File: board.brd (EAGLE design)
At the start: 50 x 50 mm, 8 parts

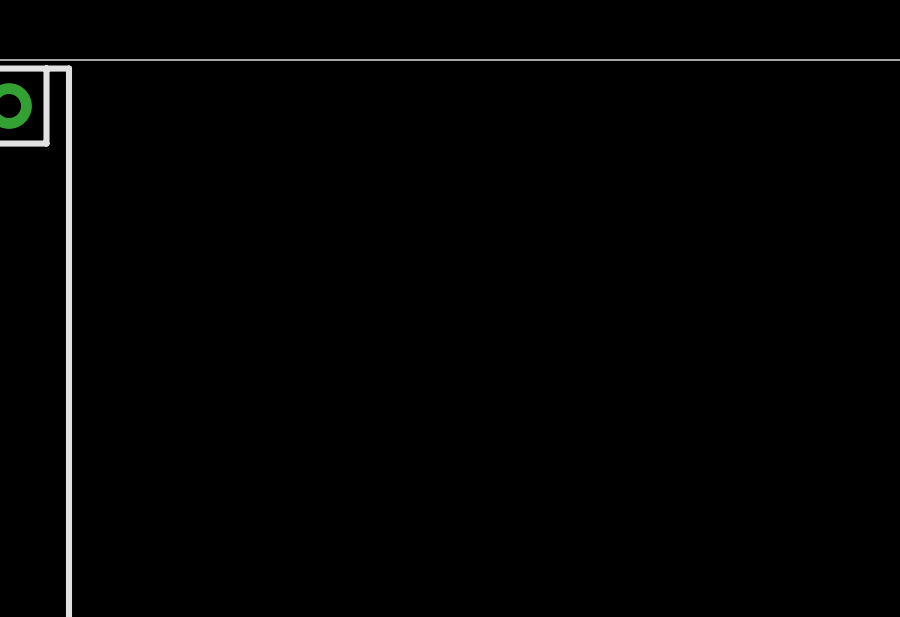
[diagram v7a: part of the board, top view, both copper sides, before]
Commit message: we have 6 HW pwm-channels, so add that many dual-mosfets
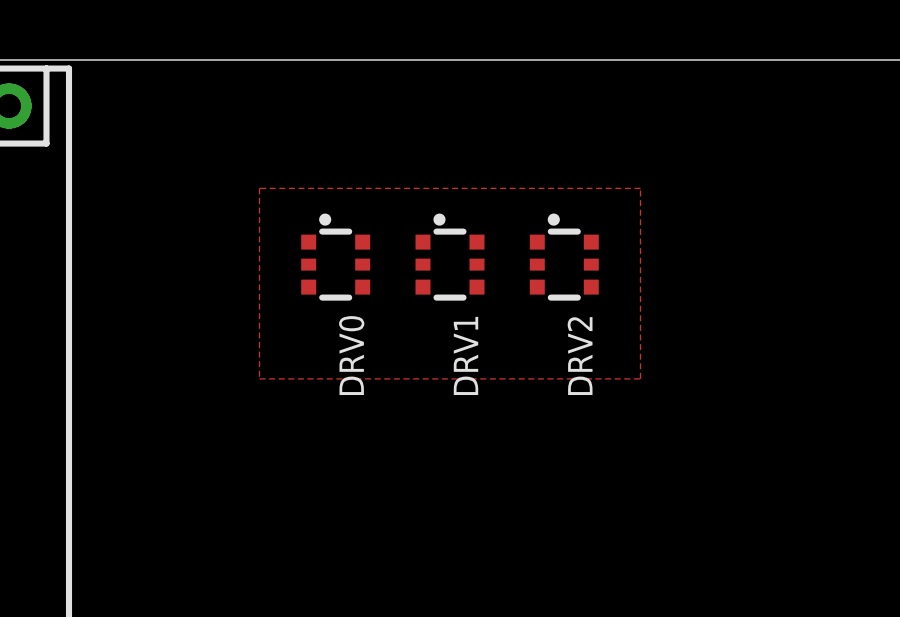
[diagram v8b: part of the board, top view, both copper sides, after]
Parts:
- added DRV0, DRV1, DRV2: (no value), microbuilder:SOT363
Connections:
- new net GND_PWR: DRV0.1, DRV0.4, DRV1.1, DRV1.4, DRV2.1, DRV2.4
- new net PWM0: DRV0.2, PORTC.1
- new net PWM1: DRV0.5, PORTC.2
- new net PWM2: DRV1.2, PORTC.3
- new net PWM3: DRV1.5, PORTC.4
- new net PWM4: DRV2.2, PORTC.5
- new net PWM5: DRV2.5, PORTC.6
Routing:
- added copper zone on layer 1, net GND_PWR
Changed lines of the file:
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@@
 <layer number="106" name="bPlate" color="7" fill="1" visible="no" active="yes"/>
 <layer number="107" name="Crop" color="7" fill="1" visible="no" active="yes"/>
+<layer number="108" name="tBridges" color="7" fill="1" visible="yes" active="yes"/>
+<layer number="109" name="tBPL" color="7" fill="1" visible="yes" active="yes"/>
+<layer number="110" name="bBPL" color="7" fill="1" visible="yes" active="yes"/>
+<layer number="111" name="MPL" color="7" fill="1" visible="yes" active="yes"/>
+<layer number="112" name="tSilk" color="7" fill="1" visible="yes" active="yes"/>
 <layer number="116" name="Patch_BOT" color="9" fill="4" visible="no" active="yes"/>
 <layer number="121" name="_tsilk" color="7" fill="1" visible="no" active="yes"/>
 <layer number="122" name="_bsilk" color="7" fill="1" visible="no" active="yes"/>
 <layer number="125" name="_tNames" color="7" fill="1" visible="no" active="yes"/>
+<layer number="126" name="_bNames" color="7" fill="1" visible="yes" active="yes"/>
+<layer number="127" name="_tValues" color="7" fill="1" visible="yes" active="yes"/>
+<layer number="128" name="_bValues" color="7" fill="1" visible="yes" active="yes"/>
 <layer number="144" name="Drill_legend" color="7" fill="1" visible="no" active="yes"/>
 <layer number="151" name="HeatSink" color="7" fill="1" visible="no" active="yes"/>
+<layer number="152" name="_bDocu" color="7" fill="1" visible="yes" active="yes"/>
 <layer number="199" name="Contour" color="7" fill="1" visible="yes" active="yes"/>
 <layer number="200" name="200bmp" color="1" fill="10" visible="no" active="yes"/>
@@
 <layer number="223" name="223bmp" color="24" fill="1" visible="no" active="no"/>
 <layer number="224" name="224bmp" color="25" fill="1" visible="no" active="no"/>
+<layer number="248" name="Housing" color="7" fill="1" visible="yes" active="yes"/>
+<layer number="249" name="Edge" color="7" fill="1" visible="yes" active="yes"/>
 <layer number="250" name="Descript" color="3" fill="1" visible="no" active="no"/>
 <layer number="251" name="SMDround" color="12" fill="11" visible="no" active="no"/>
@@
 <classes>
 <class number="0" name="default" width="0" drill="0">
+</class>
+<class number="1" name="PWR" width="0.4064" drill="0">
 </class>
 </classes>
@@
 </element>
 <element name="PWR_STACK" library="SparkFun-Connectors" package="1X03" value="" x="1.27" y="3.81" locked="yes" rot="R90"/>
+<element name="DRV0" library="microbuilder" package="SOT363" value="" x="30.48" y="43.18" rot="R270"/>
+<element name="DRV1" library="microbuilder" package="SOT363" value="" x="34.29" y="43.18" rot="R270"/>
+<element name="DRV2" library="microbuilder" package="SOT363" value="" x="38.1" y="43.18" rot="R270"/>
 </elements>
 <signals>
-<signal name="GND">
+<signal name="GND" class="1">
 <contactref element="XBEE" pad="10"/>
 <contactref element="PORTD" pad="7"/>
@@
 <contactref element="PDI_STACK" pad="6"/>
 <contactref element="PWR_STACK" pad="2"/>
-<wire x1="43.18" y1="1.27" x2="19.59" y2="26.465" width="0" layer="19" extent="1-1"/>
 <wire x1="40.64" y1="1.27" x2="43.18" y2="1.27" width="0" layer="19" extent="1-1"/>
-<wire x1="5.715" y1="8.89" x2="40.64" y2="1.27" width="0" layer="19" extent="1-1"/>
+<wire x1="19.59" y1="26.465" x2="40.64" y2="1.27" width="0" layer="19" extent="1-1"/>
+<wire x1="5.715" y1="8.89" x2="19.59" y2="26.465" width="0" layer="19" extent="1-1"/>
 <wire x1="1.27" y1="6.35" x2="5.715" y2="8.89" width="0" layer="19" extent="1-1"/>
 </signal>
@@
 <contactref element="PORTC" pad="7"/>
 </signal>
+<signal name="GND_PWR" class="1">
+<contactref element="DRV0" pad="1"/>
+<contactref element="DRV0" pad="4"/>
+<contactref element="DRV1" pad="4"/>
+<contactref element="DRV2" pad="4"/>
+<contactref element="DRV2" pad="1"/>
+<contactref element="DRV1" pad="1"/>
+<polygon width="0.4064" layer="1" isolate="0.254" rank="6">
+<vertex x="27.94" y="45.72"/>
+<vertex x="27.94" y="39.37"/>
+<vertex x="40.64" y="39.37"/>
+<vertex x="40.64" y="45.72"/>
+</polygon>
+</signal>
+<signal name="PWM0">
+<contactref element="PORTC" pad="1"/>
+<contactref element="DRV0" pad="2"/>
+<wire x1="5.08" y1="1.27" x2="29.58" y2="43.18" width="0" layer="19" extent="1-1"/>
+</signal>
+<signal name="PWM1">
+<contactref element="PORTC" pad="2"/>
+<contactref element="DRV0" pad="5"/>
+<wire x1="7.62" y1="1.27" x2="31.38" y2="43.18" width="0" layer="19" extent="1-1"/>
+</signal>
+<signal name="PWM2">
+<contactref element="PORTC" pad="3"/>
+<contactref element="DRV1" pad="2"/>
+<wire x1="10.16" y1="1.27" x2="33.39" y2="43.18" width="0" layer="19" extent="1-1"/>
+</signal>
+<signal name="PWM3">
+<contactref element="PORTC" pad="4"/>
+<contactref element="DRV1" pad="5"/>
+<wire x1="12.7" y1="1.27" x2="35.19" y2="43.18" width="0" layer="19" extent="1-1"/>
+</signal>
+<signal name="PWM4">
+<contactref element="PORTC" pad="5"/>
+<contactref element="DRV2" pad="2"/>
+<wire x1="15.24" y1="1.27" x2="37.2" y2="43.18" width="0" layer="19" extent="1-1"/>
+</signal>
+<signal name="PWM5">
+<contactref element="PORTC" pad="6"/>
+<contactref element="DRV2" pad="5"/>
+<wire x1="17.78" y1="1.27" x2="39" y2="43.18" width="0" layer="19" extent="1-1"/>
+</signal>
 </signals>
